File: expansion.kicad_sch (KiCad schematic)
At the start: 45 parts, among them IC10 GAL16V8, IC11 74LS367ADR, IC12 74LS367ADR, IC13 74LS368AD, IC14 74LS367ADR, IC15 74ALS30ADR, IC16 74LS245DWR, IC17 74LS367ADR, IC18 74LS139ADR, IC19 74LS153DR, IC20 74LS374DWR, IC21 74LS367ADR, IC22 74LS74ADR, J10 CARTRIDGE EDGE, J12 CARTRIDGE EDGE, J13 CARTRIDGE EDGE, J9 CARTRIDGE EDGE, SW3 DEFAULT SLOT

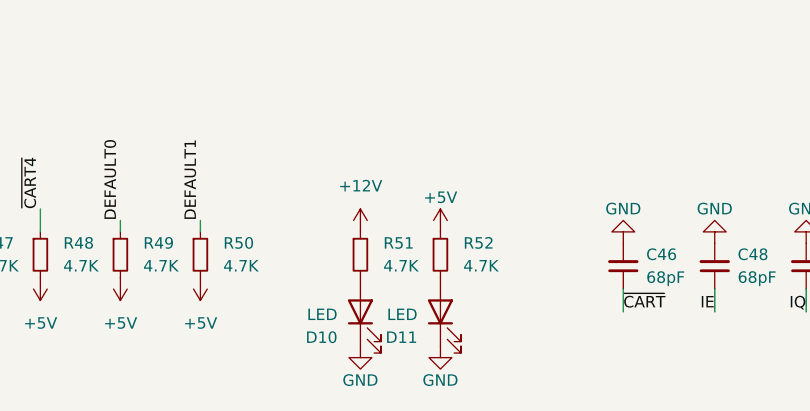
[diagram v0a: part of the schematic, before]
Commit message: shrink board in the wash
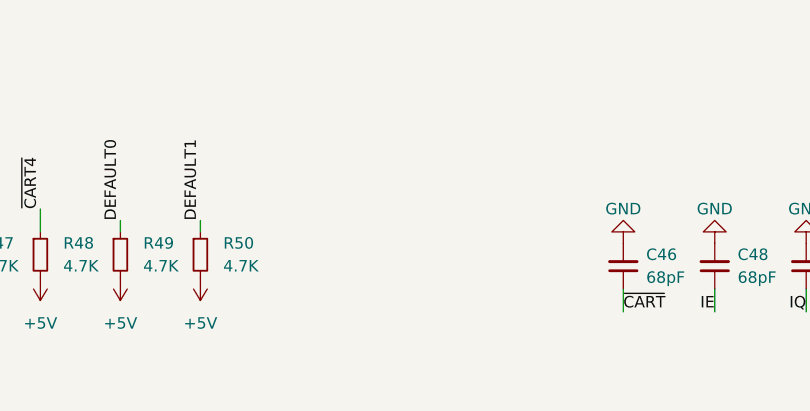
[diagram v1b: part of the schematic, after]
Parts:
- removed D10, D11: LED, LED_SMD:LED_0805_2012Metric_Pad1.15x1.40mm_HandSolder, symbol Device:LED
- removed R51, R52: 4.7K, Resistor_SMD:R_0805_2012Metric_Pad1.20x1.40mm_HandSolder, symbol Device:R_Small

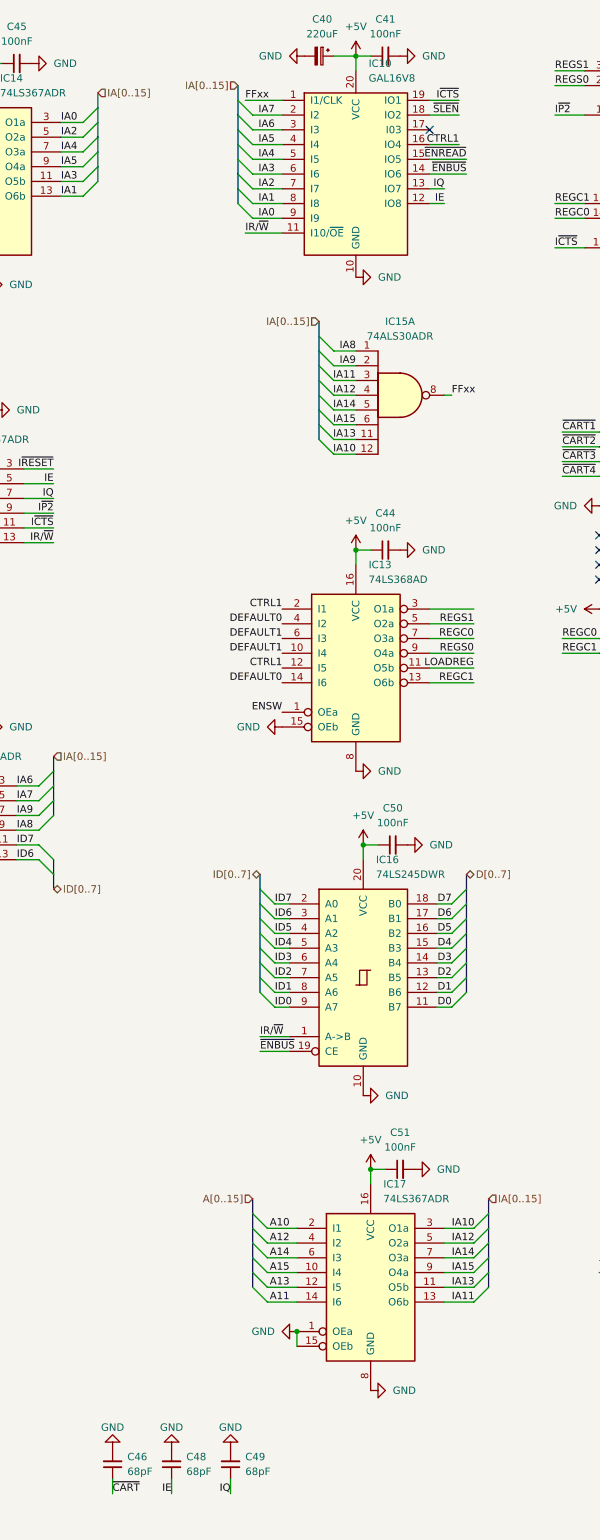
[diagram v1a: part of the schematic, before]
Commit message: rework to flex atx size
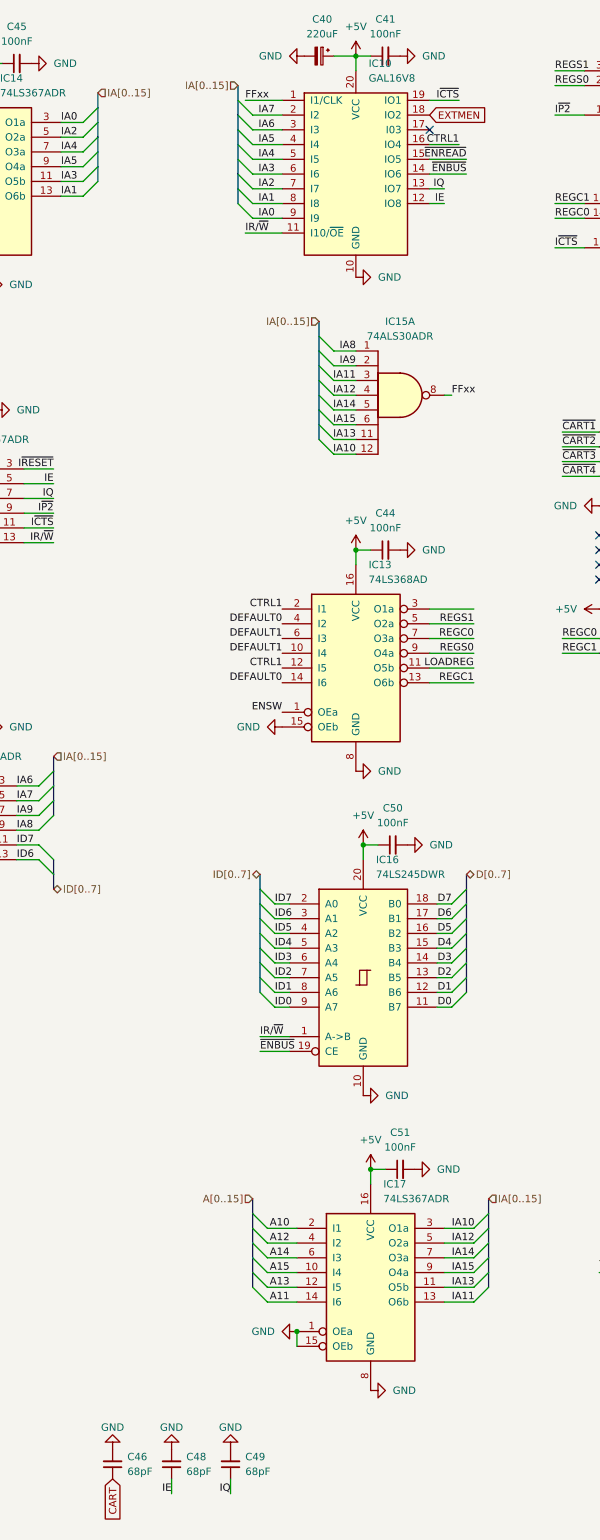
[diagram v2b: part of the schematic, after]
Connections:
- net ~{CART} is gone; now on net CART: C46.1
- net ~{SLEN} is gone; now on net EXTMEN: IC10.18 (IO2)
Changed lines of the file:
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@@
 	(wire
 		(pts
-			(xy 294.64 34.29) (xy 299.72 34.29)
-		)
-		(stroke
-			(width 0)
-			(type default)
-		)
-	)
-	(wire
-		(pts
 			(xy 66.04 167.64) (xy 69.85 167.64)
 		)
@@
 	(wire
 		(pts
-			(xy 240.03 269.24) (xy 240.03 271.78)
-		)
-		(stroke
-			(width 0)
-			(type default)
-		)
-	)
-	(wire
-		(pts
 			(xy 336.55 172.72) (xy 344.17 172.72)
 		)
@@
 		)
 	)
-	(label "~{CART}"
-		(at 240.03 271.78 0)
-		(fields_autoplaced yes)
-		(effects
-			(font
-				(size 1.27 1.27)
-			)
-			(justify left bottom)
-		)
-	)
 	(label "IA1"
 		(at 66.04 198.12 0)
@@
 		)
 	)
-	(label "~{SLEN}"
-		(at 299.72 34.29 180)
-		(fields_autoplaced yes)
-		(effects
-			(font
-				(size 1.27 1.27)
-			)
-			(justify right bottom)
-		)
-	)
 	(label "ID1"
 		(at 116.84 95.25 0)
@@
 		)
 	)
+	(global_label "CART"
+		(shape input)
+		(at 240.03 269.24 270)
+		(fields_autoplaced yes)
+		(effects
+			(font
+				(size 1.27 1.27)
+			)
+			(justify right)
+		)
+		(property "Intersheetrefs" "${INTERSHEET_REFS}"
+			(at 240.03 276.8214 90)
+			(effects
+				(font
+					(size 1.27 1.27)
+				)
+				(justify right)
+				(hide yes)
+			)
+		)
+	)
 	(global_label "~{HALT}"
 		(shape input)
@@
 				(hide yes)
 			)
+		)
+	)
+	(global_label "EXTMEN"
+		(shape input)
+		(at 294.64 34.29 0)
+		(fields_autoplaced yes)
+		(effects
+			(font
+				(size 1.27 1.27)
+			)
+			(justify left)
+		)
+		(property "Intersheetrefs" "${INTERSHEET_REFS}"
+			(at 304.8822 34.29 0)
+			(effects
+				(font
+					(size 1.27 1.27)
+				)
+				(justify left)
+				(hide yes)
+			)

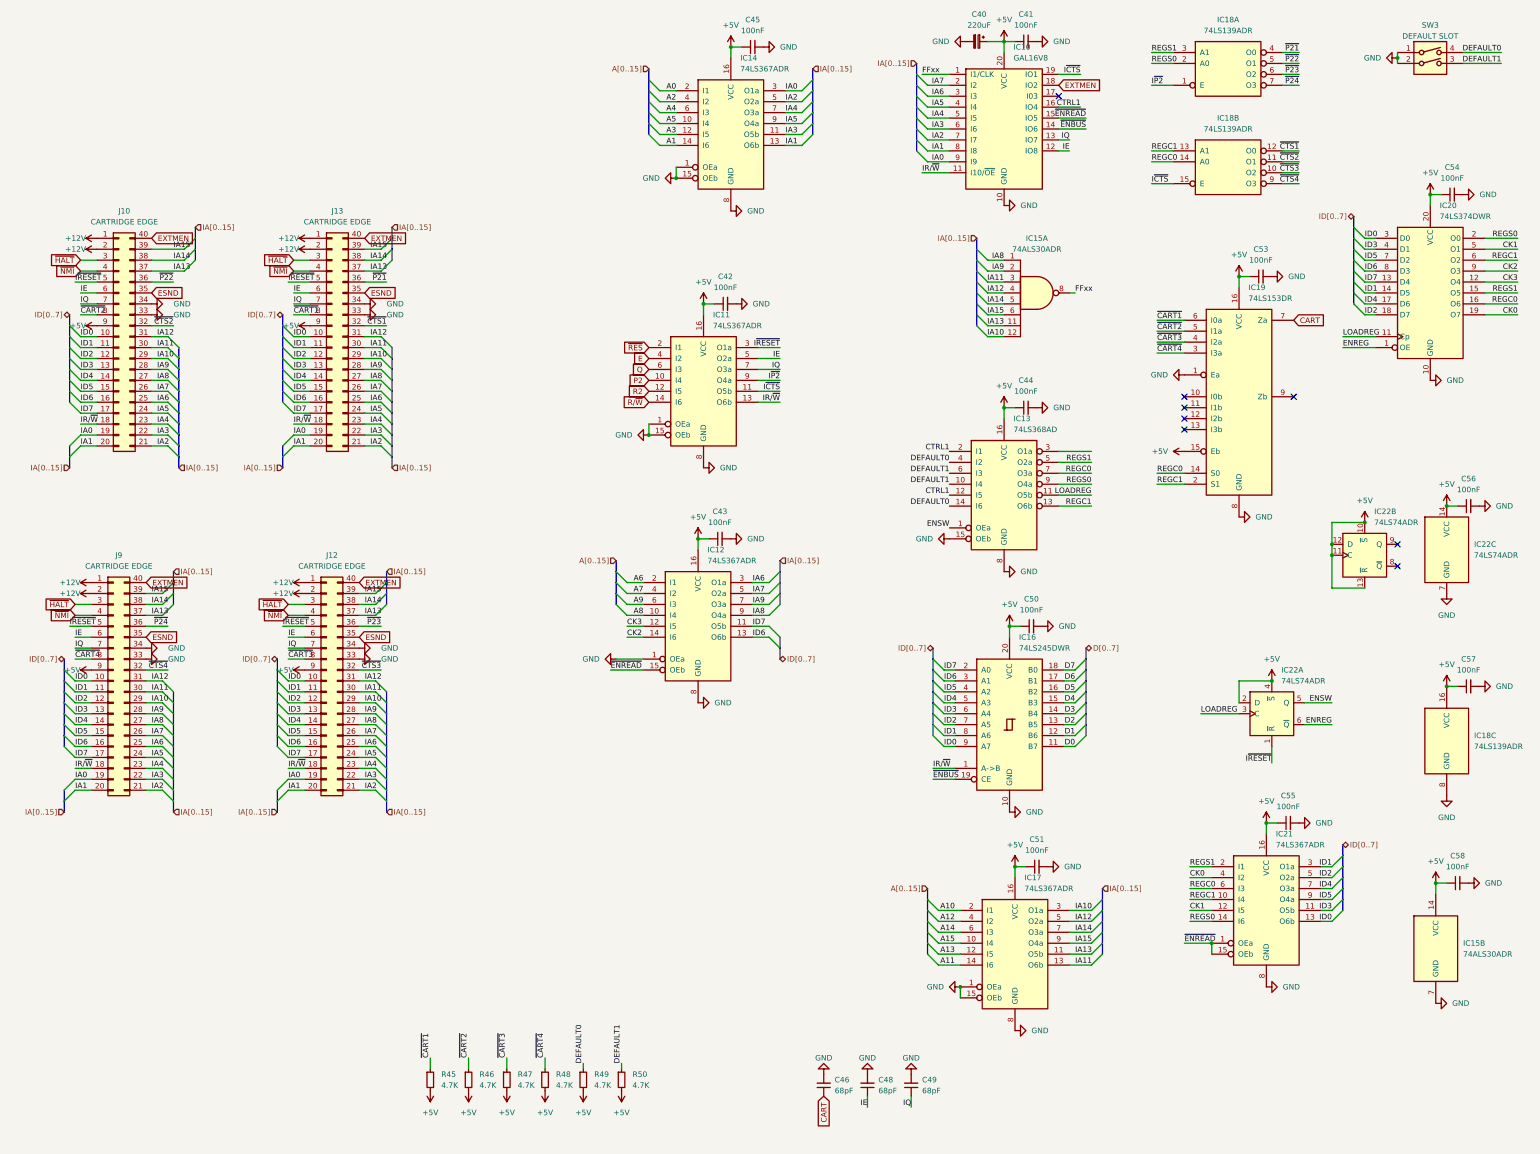
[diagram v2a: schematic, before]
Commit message: complete routing
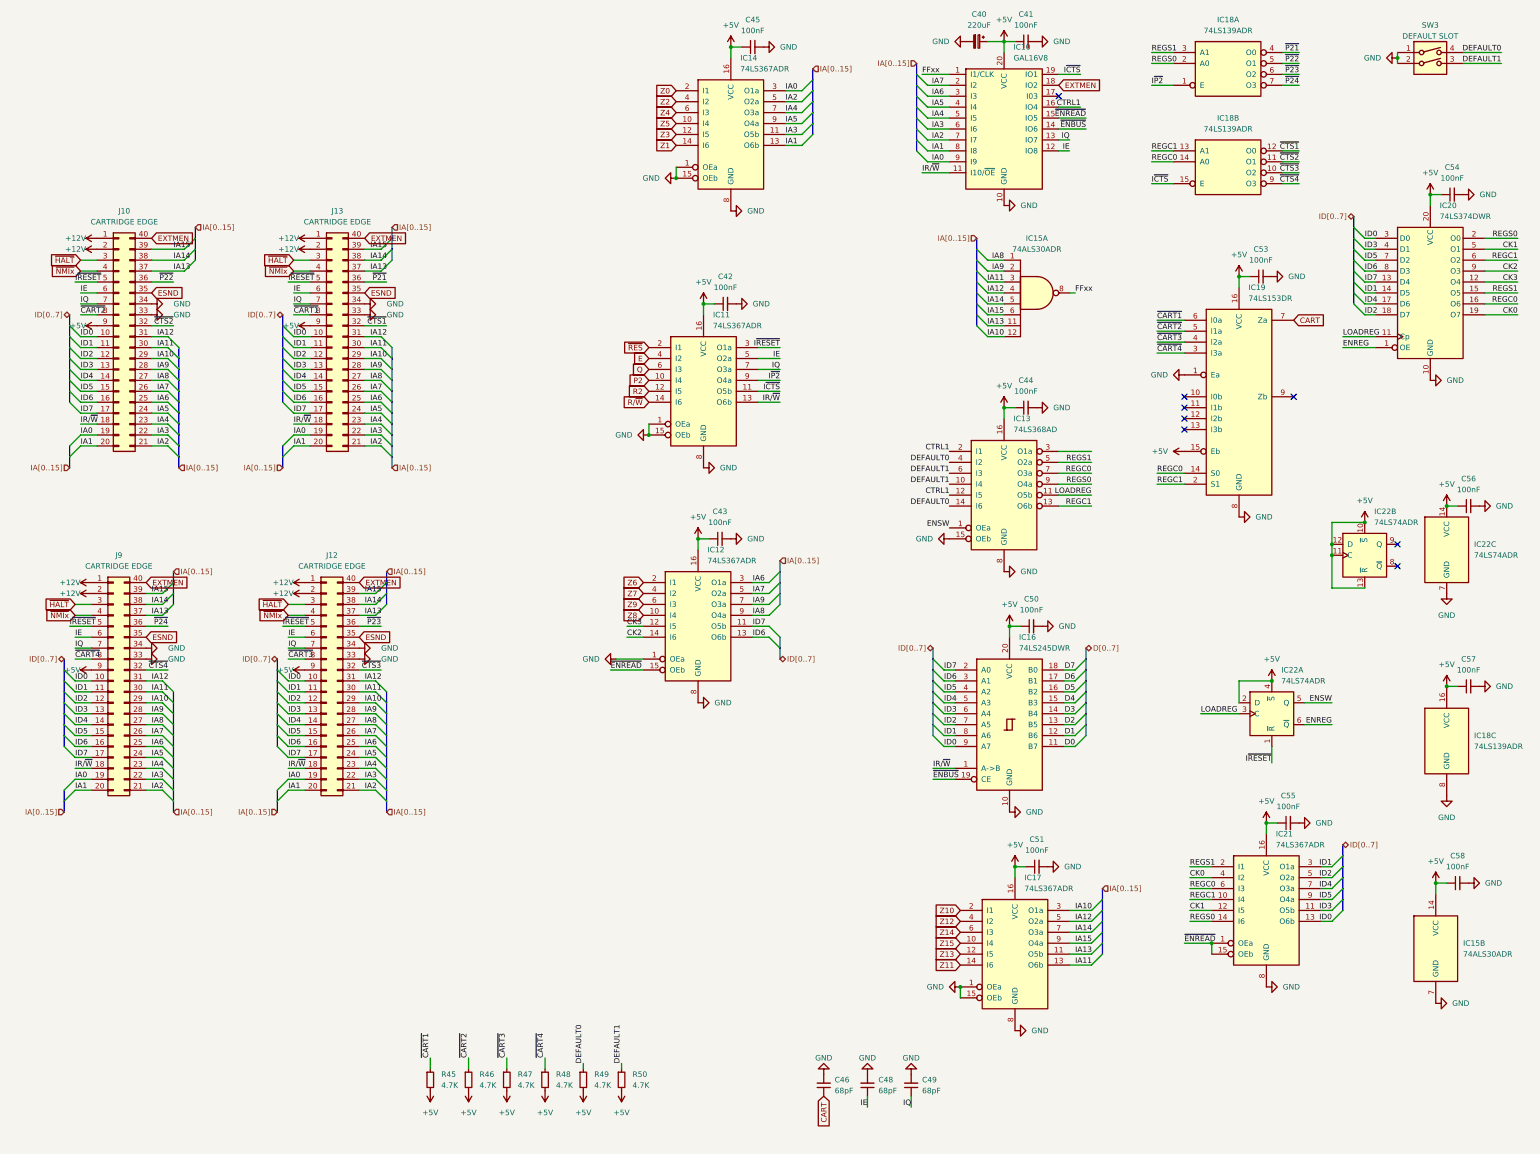
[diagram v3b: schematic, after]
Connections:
- net A0 renamed Z0
- net A1 renamed Z1
- net A10 renamed Z10
- net A11 renamed Z11
- net A12 renamed Z12
- net A13 renamed Z13
- net A14 renamed Z14
- net A15 renamed Z15
- net A2 renamed Z2
- net A3 renamed Z3
- net A4 renamed Z4
- net A5 renamed Z5
- net A6 renamed Z6
- net A7 renamed Z7
- net A8 renamed Z8
- net A9 renamed Z9
- net ~{NMI} renamed ~{NMIx}

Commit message: update vendor specific BOM fields
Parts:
- J10, J12, J13, J9: DigiKey (none) -> S3315-ND
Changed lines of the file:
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@@
 			)
 		)
+		(property "DigiKey" "S3315-ND"
+			(at 76.2 92.71 0)
+			(effects
+				(font
+					(size 1.27 1.27)
+				)
+				(hide yes)
+			)
+		)
 		(pin "13"
 		)
@@
 			)
 		)
+		(property "DigiKey" "S3315-ND"
+			(at 124.46 172.72 0)
+			(effects
+				(font
+					(size 1.27 1.27)
+				)
+				(hide yes)
+			)
+		)
 		(pin "13"
 		)
@@
 			)
 		)
+		(property "DigiKey" "S3315-ND"
+			(at 74.93 172.72 0)
+			(effects
+				(font
+					(size 1.27 1.27)
+				)
+				(hide yes)
+			)
+		)
 		(pin "13"
 		)
@@
 			(at 125.73 92.71 0)
 			(effects
+				(font
+					(size 1.27 1.27)
+				)
+				(hide yes)
+			)
+		)
+		(property "DigiKey" "S3315-ND"
+			(at 125.73 92.71 0)
+			(effects
